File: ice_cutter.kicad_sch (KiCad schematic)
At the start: 92 parts, among them J1 Conn_01x01_Male, J2 Barrel_Jack, J3 Conn_01x03_Male, J4 Conn_01x01_Male, J5 Conn_02x03_Odd_Even, M1 Motor_Servo, M2 Motor_Servo, Q1 Q_PMOS_GSD, Q10 Q_NPN_EBC, Q11 Q_NMOS_GSD, Q2 Q_PMOS_GSD, Q3 Q_PMOS_GSD, Q4 Q_PNP_EBC, Q5 Q_NMOS_GSD, Q6 Q_PNP_EBC, Q7 Q_NMOS_GSD, Q8 Q_NPN_EBC, Q9 Q_NPN_EBC, SW1 SW_Push, SW2 SW_Push, SW3 SW_Push, U1 LM317_TO-252, U10 TMP117, U11 TM1620, U2 LM317_TO-252, U3 INA219AxD, U4 LM317_TO-252, U5 INA219AxD, U6 FJ4301AH, U7 FJ4301AH, U8 STM32G030XX, U9 SHT30-DIS

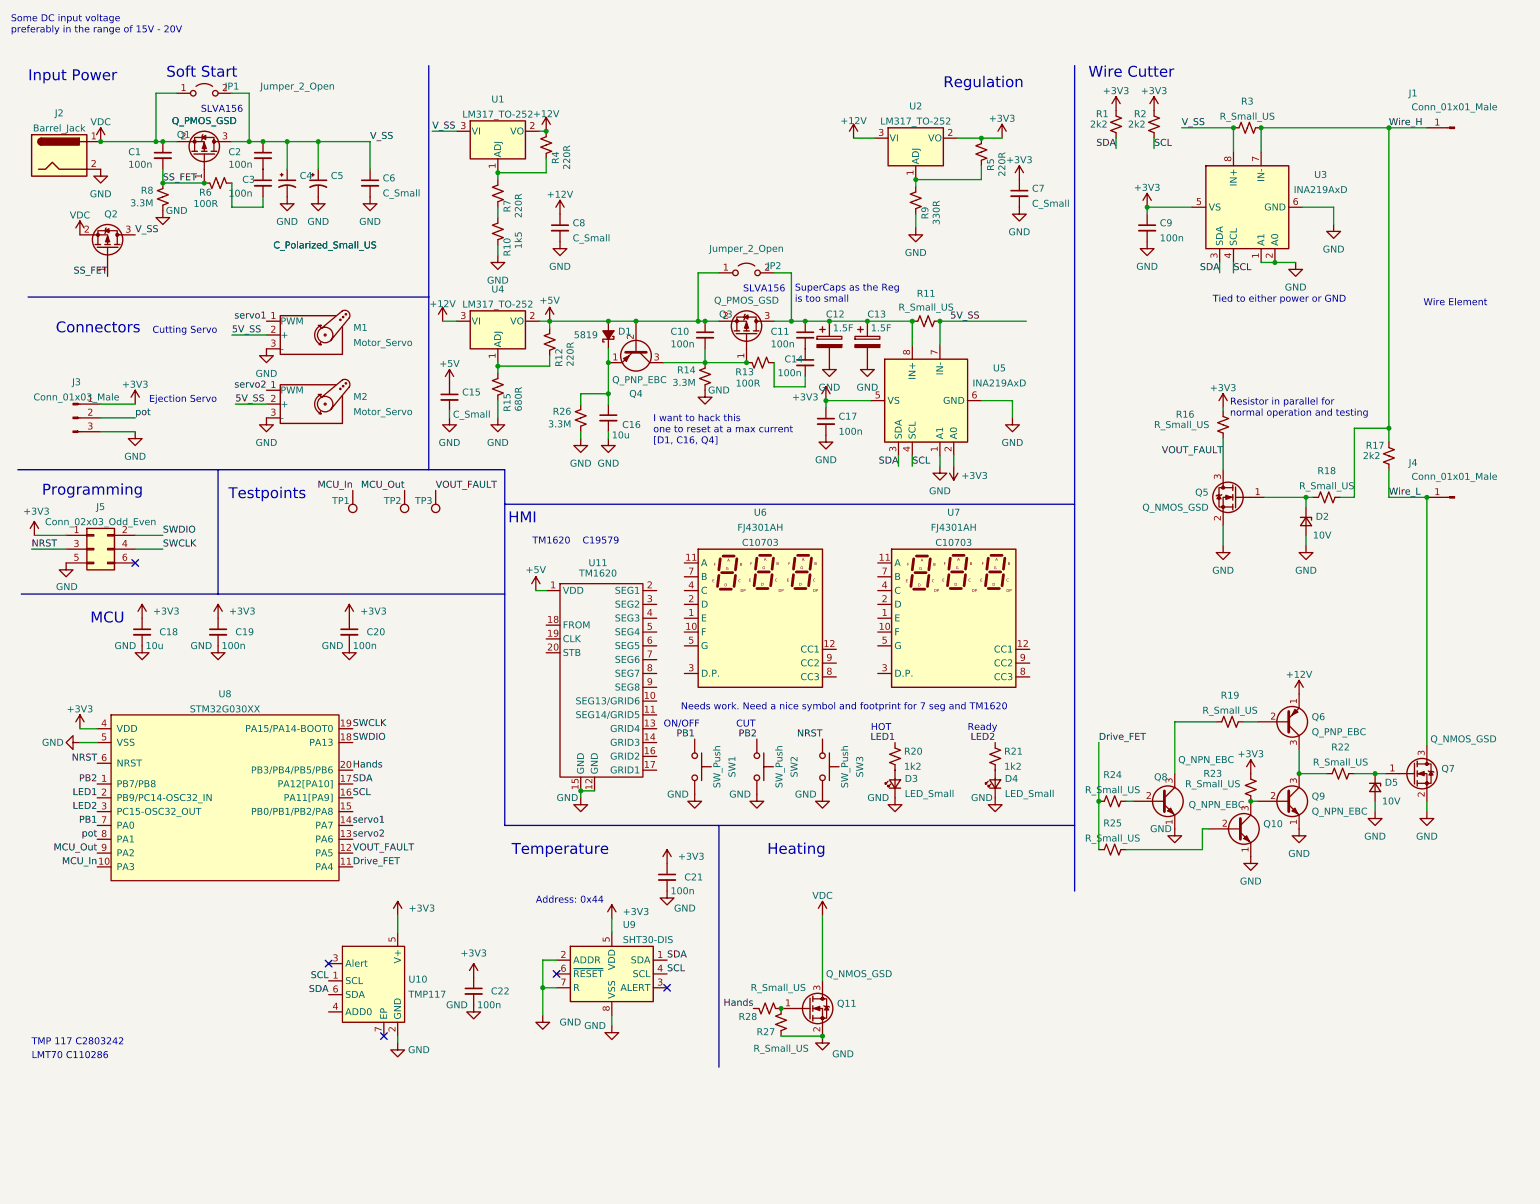
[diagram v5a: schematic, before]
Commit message: added some TP and some 0R resistors and a program header for simple programming
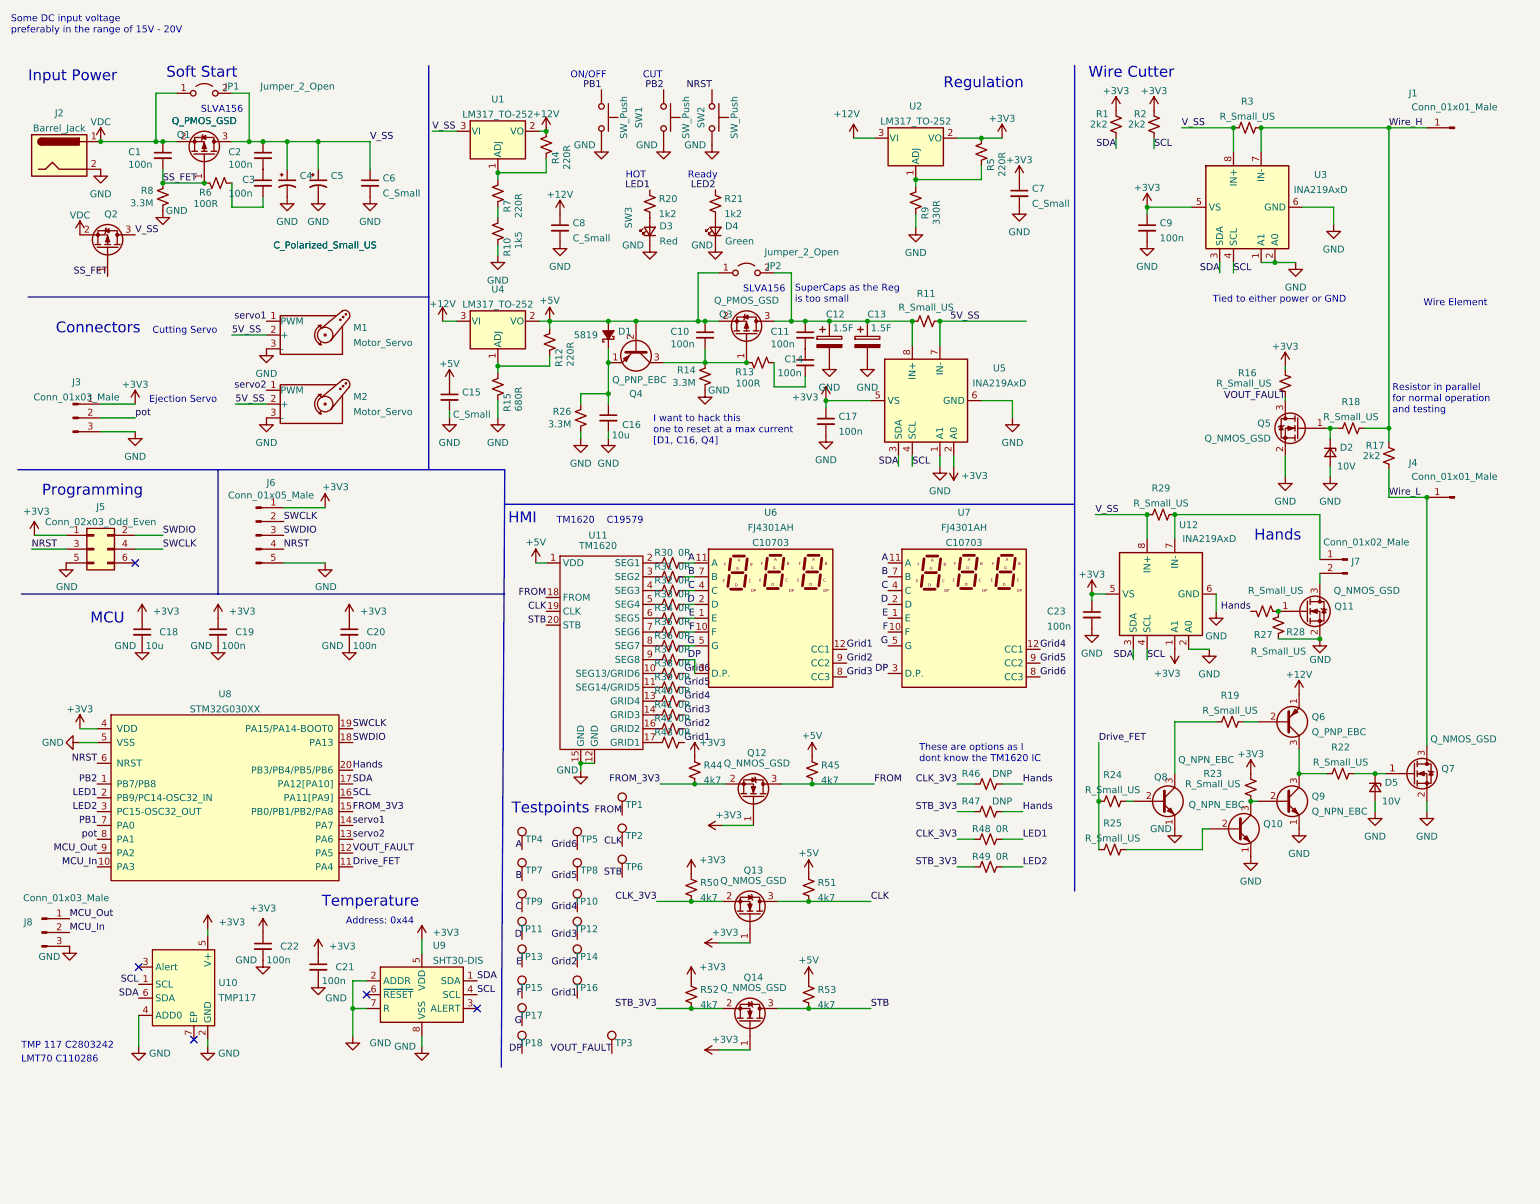
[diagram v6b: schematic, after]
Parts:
- added C23: 100n, symbol Device:C_Small
- added J6: Conn_01x05_Male, Connector_PinHeader_2.54mm:PinHeader_1x05_P2.54mm_Vertical, symbol Connector:Conn_01x05_Male
- added J7: Conn_01x02_Male, symbol Connector:Conn_01x02_Male
- added J8: Conn_01x03_Male, symbol Connector:Conn_01x03_Male
- added Q12, Q13, Q14: Q_NMOS_GSD, Package_TO_SOT_SMD:SOT-23, symbol Device:Q_NMOS_GSD
- added R29: R_Small_US, Resistor_SMD:R_0402_1005Metric, symbol Device:R_Small_US
- added R30, R31, R32, R33, R34, R35, R36, R37, R38, R39, R40, R41, R42, R43, R48, R49: 0R, Resistor_SMD:R_0402_1005Metric, symbol Device:R_Small_US
- added R44, R45, R50, R51, R52, R53: 4k7, Resistor_SMD:R_0402_1005Metric, symbol Device:R_Small_US
- added R46, R47: DNP, Resistor_SMD:R_0402_1005Metric, symbol Device:R_Small_US
- added TP10, TP11, TP12, TP13, TP14, TP15, TP16, TP17, TP18, TP4, TP5, TP6, TP7, TP8, TP9: TestPoint, TestPoint:TestPoint_Pad_D2.0mm, symbol Connector:TestPoint
- added U12: INA219AxD, Package_SO:SOIC-8_3.9x4.9mm_P1.27mm, symbol Analog_ADC:INA219AxD
- D3: value LED_Small -> Red
- D4: value LED_Small -> Green; LCSC C2286 -> C720XX
- U11: Extended (none) -> 1; LCSC (none) -> C19579; Price (none) -> 0
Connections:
- net +3V3: now also C23.1, J6.1 (Pin_1), Q12.1 (G), Q13.1 (G), Q14.1 (G), R44.1, R50.1, R52.1, U12.1 (A1), U12.5 (VS)
- net +5V: now also R45.2, R51.2, R53.2
- net GND: now also U10.4 (ADD0), C23.2, J6.5 (Pin_5), J8.3 (Pin_3), U12.2 (A0), U12.6 (GND)
- net Hands: now also R46.2, R47.2
- net LED1: now also R48.2
- net LED2: now also R49.2
- net MCU_In: now also J8.2 (Pin_2); no longer TP1.1
- net MCU_Out: now also J8.1 (Pin_1); no longer TP2.1
- net NRST: now also J6.4 (Pin_4)
- net SCL: now also U12.4 (SCL)
- net SDA: now also U12.3 (SDA)
- net SWCLK: now also J6.2 (Pin_2)
- net SWDIO: now also J6.3 (Pin_3)
- net VDC: no longer Q11.3 (D)
- net V_SS: now also R29.1, U12.8 (IN+)
- net E: now reaches U7.1 (E)
- net E: now also U6.1 (E), R34.2, TP13.1
- net F: now reaches U7.10 (F)
- net F: now also U6.10 (F), R35.2, TP15.1
- net A: now reaches U7.11 (A)
- net A: now also U6.11 (A), R30.2, TP4.1
- net Grid4: now reaches U7.12 (CC1)
- net Grid4: now also R40.2, TP10.1
- net D: now reaches U7.2 (D)
- net D: now also U6.2 (D), R33.2, TP11.1
- net DP: now reaches U7.3 (D.P.)
- net DP: now also U6.3 (D.P.), R37.2, TP18.1
- net C: now reaches U7.4 (C)
- net C: now also U6.4 (C), R32.2, TP9.1
- net G: now reaches U7.5 (G)
- net G: now also U6.5 (G), R36.2, TP17.1
- net B: now reaches U7.7 (B)
- net B: now also U6.7 (B), R31.2, TP7.1
- net Grid6: now reaches U7.8 (CC3)
- net Grid6: now also R38.2, TP5.1
- net Grid5: now reaches U7.9 (CC2)
- net Grid5: now also R39.2, TP8.1
- net at U11.10 (SEG13/GRID6): now also R38.1
- net at U11.11 (SEG14/GRID5): now also R39.1
- net at U11.13 (GRID4): now also R40.1
- net at U11.14 (GRID3): now also R41.1
- net at U11.16 (GRID2): now also R42.1
- net at U11.17 (GRID1): now also R43.1
- net FROM: now reaches U11.18 (FROM)
- net FROM: now also TP1.1, Q12.3 (D), R45.1
- net CLK: now reaches U11.19 (CLK)
- net CLK: now also TP2.1, Q13.3 (D), R51.1
- net at U11.2 (SEG1): now also R30.1
- net STB: now reaches U11.20 (STB)
- net STB: now also Q14.3 (D), R53.1, TP6.1
- net at U11.3 (SEG2): now also R31.1
- net at U11.4 (SEG3): now also R32.1
- net at U11.5 (SEG4): now also R33.1
- net at U11.6 (SEG5): now also R34.1
- net at U11.7 (SEG6): now also R35.1
- net at U11.8 (SEG7): now also R36.1
- net at U11.9 (SEG8): now also R37.1
- net Grid1: now reaches U6.12 (CC1)
- net Grid1: now also R43.2, TP16.1
- net Grid3: now reaches U6.8 (CC3)
- net Grid3: now also R41.2, TP12.1
- net Grid2: now reaches U6.9 (CC2)
- net Grid2: now also R42.2, TP14.1
- net FROM_3V3: now reaches U8.15 (PB0/PB1/PB2/PA8)
- net FROM_3V3: now also Q12.2 (S), R44.2
- new net: J7.1 (Pin_1), R29.2, U12.7 (IN-)
- new net: J7.2 (Pin_2), Q11.3 (D)
- new net CLK_3V3: Q13.2 (S), R46.1, R48.1, R50.2
- new net STB_3V3: Q14.2 (S), R47.1, R49.1, R52.2
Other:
- note added: "Hands"
- note added: "These are options as I dont know the TM1620 IC"
- note removed: "Heating"
- note removed: "Needs work. Need a nice symbol and footprint for 7 seg and TM1620"
- moved on the sheet: C21, C22, D2, D3, D4, Q11, Q5, R16, R18, R20, R21, R27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

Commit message: added more TP
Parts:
- added TP19, TP20, TP21, TP22, TP23, TP24, TP25, TP26, TP27, TP28, TP29, TP30, TP31, TP32, TP33, TP34: TestPoint, TestPoint:TestPoint_Pad_D2.0mm, symbol Connector:TestPoint
- Q11: footprint (none) -> Package_TO_SOT_SMD:TO-252-2; Extended (none) -> 1; LCSC (none) -> C130980; Price (none) -> 0.2
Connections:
- net +3V3: now also TP23.1
- net +5V: now also TP21.1
- net 5V_SS: now also TP22.1
- net Drive_FET: now also TP32.1
- net GND: now also TP27.1, TP28.1, TP29.1
- net SCL: now also TP31.1
- net SDA: now also TP30.1
- net VDC: now also TP19.1
- net V_SS: now also TP20.1
- net Wire_H: now also TP25.1
- net Wire_L: now also TP26.1
- net servo1: now also TP33.1
- net servo2: now also TP34.1
- net SS_FET2: now reaches C10.2, Q3.1 (G), Q4.3 (C), R13.1, R14.1
- net AUTO_RESTART: now reaches C16.1, D1.1 (K), Q4.1 (E), R26.1
- net FET_GATE: now reaches D5.1 (K), Q7.1 (G), R22.2
- net FET_GATE: now also TP24.1
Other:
- moved on the sheet: Q12, Q13, Q14, R44, R45, R50, R51, R52, R53

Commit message: Think I have finished the schematic
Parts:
- removed Q10, Q8, Q9: Q_NPN_EBC, symbol Device:Q_NPN_EBC
- removed Q4, Q6: Q_PNP_EBC, symbol Device:Q_PNP_EBC
- removed R19, R22, R23, R24, R25, R27, R28: R_Small_US, Resistor_SMD:R_0402_1005Metric, symbol Device:R_Small_US
- added J9: xt60, UCT:XT60PW-M, symbol Connector:Conn_01x02_Male
- added JP3: Jumper_2_Open, Jumper:SolderJumper-2_P1.3mm_Open_RoundedPad1.0x1.5mm, symbol Jumper:Jumper_2_Open
- added Q4: S8550, Package_TO_SOT_SMD:SOT-23, symbol MyDevices:S8550
- added RV1: 10k, UCT:RK09_THT_Pot_C209770, symbol Device:R_Potentiometer_US
- C1, C10, C11, C14, C18, C19, C2, C20, C21, C22, C3, D3, JP1, JP2, M1, M2, Q1, Q12, Q13, Q14, Q2, Q3, R10, R12, R13, R14, R15, R26, R4, R44, R45, R5, R50, R51, R52, R53, R6, R7, R8, R9, U8: Extended (none) -> 0
- C12, C13, U6, U7, U9: Extended (none) -> 1
- C15, C6, C7, C8: value C_Small -> 10u; footprint (none) -> Capacitor_SMD:C_0603_1608Metric; Extended (none) -> 0; LCSC (none) -> C96446; Price (none) -> 0.03
- C16: footprint (none) -> Capacitor_SMD:C_0603_1608Metric; Extended (none) -> 0; LCSC (none) -> C96446; Price (none) -> 0.03
- C17, C23, C9: footprint (none) -> Capacitor_SMD:C_0402_1005Metric; Extended (none) -> 0; LCSC (none) -> C307331; Price (none) -> 0.006
- C4, C5: value C_Polarized_Small_US -> 1m; footprint (none) -> Capacitor_THT:CP_Radial_D14.0mm_P5.00mm; Extended (none) -> 1; Populate Yes -> No
- D1: Extended (none) -> 0; LCSC (none) -> C963381; Price (none) -> 0.009
- D4: Extended (none) -> 0; LCSC C720XX -> C72043
- J1, J4: footprint Connector_PinHeader_2.54mm:PinHeader_1x01_P2.54mm_Vertical -> MyLibs:SMD_Pad_15x10; Extended (none) -> 0
- J3: value Conn_01x03_Male -> pot; Extended (none) -> 0
- J5: value Conn_02x03_Odd_Even -> program; Extended (none) -> 0
- J6: value Conn_01x05_Male -> program2; Extended (none) -> 0; Populate (none) -> No
- J7: value Conn_01x02_Male -> hands; footprint (none) -> Connector_PinHeader_2.54mm:PinHeader_1x02_P2.54mm_Vertical; Extended (none) -> 0; Populate (none) -> No
- J8: value Conn_01x03_Male -> UART; footprint (none) -> Connector_PinHeader_2.54mm:PinHeader_1x03_P2.54mm_Vertical; Extended (none) -> 0; Populate (none) -> No
- Q5: footprint (none) -> Package_TO_SOT_SMD:SOT-23; Extended (none) -> 0; LCSC (none) -> C20917; Price (none) -> 0.23
- R1, R17, R2: value 2k2 -> 4k7; Extended (none) -> 0; LCSC (none) -> C25900; Price (none) -> 0.0007
- R11, R29, R3: value R_Small_US -> 0R1; footprint Resistor_SMD:R_0402_1005Metric -> Resistor_SMD:R_1206_3216Metric; Extended (none) -> 0; LCSC (none) -> C25334; Price (none) -> 0.0087
- R16: value R_Small_US -> 4k7; Extended (none) -> 0; LCSC (none) -> C25900; Price (none) -> 0.0007
- R18: value R_Small_US -> 100R; Extended (none) -> 0; LCSC (none) -> C25076; Price (none) -> 0.0007
- R20, R21: value 1k2 -> 1k5; Extended (none) -> 0; LCSC (none) -> C25867; Price (none) -> 0.0007
- U10: footprint (none) -> Package_SON:WSON-6-1EP_2x2mm_P0.65mm_EP1x1.6mm; Extended (none) -> 1; LCSC (none) -> C2803242; Price (none) -> 3.25
- U12, U3, U5: Extended (none) -> 1; LCSC (none) -> C138706; Price (none) -> 1.62
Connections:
- net +3V3: now also RV1.1
- net +5V: now also Q4.1 (B)
- net AUTO_RESTART: now also Q4.2 (E)
- net FET_GATE: no longer D5.1 (K)
- net GND: now also J9.2 (Pin_2), RV1.3; no longer D5.2 (A)
- net SS_FET: now also D5.2 (A)
- net SS_FET2: now also Q4.3 (C)
- net VDC: now also D5.1 (K), J9.1 (Pin_1)
- net pot: now also JP3.1 (A)
- net FET_Drive1/Drive_Out: now reaches Q11.1 (G)
- new net: JP3.2 (B), RV1.2
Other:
- added sheet FET_Drive (FET_Drive_sch.kicad_sch)
- added sheet FET_Drive1 (FET_Drive_sch.kicad_sch)
- note added: "Address: 1 0 0 1 0 0 0 --> ADD0 GND Address: 1 0 0 1 0 0 1 --> ADD0 V+ Address: 1 0 0 1 0 1 0 --> ADD0 SDA Address: 1 0 0 1 0 1 1 --> ADD0 SCL"
- note added: "XT60 for funzies"
- moved on the sheet: C1, J7, Q11, R8
